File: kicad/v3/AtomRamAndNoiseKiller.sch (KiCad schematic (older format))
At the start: 26 parts, among them J1 Conn_01x10, J2 Conn_01x10, J3 Conn_01x03, J4 Conn_01x09, J5 Conn_01x09, J6 Conn_01x03, U1 74HCT14, U2 74HCT08, U3 74HCT245, U4 74HCT573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

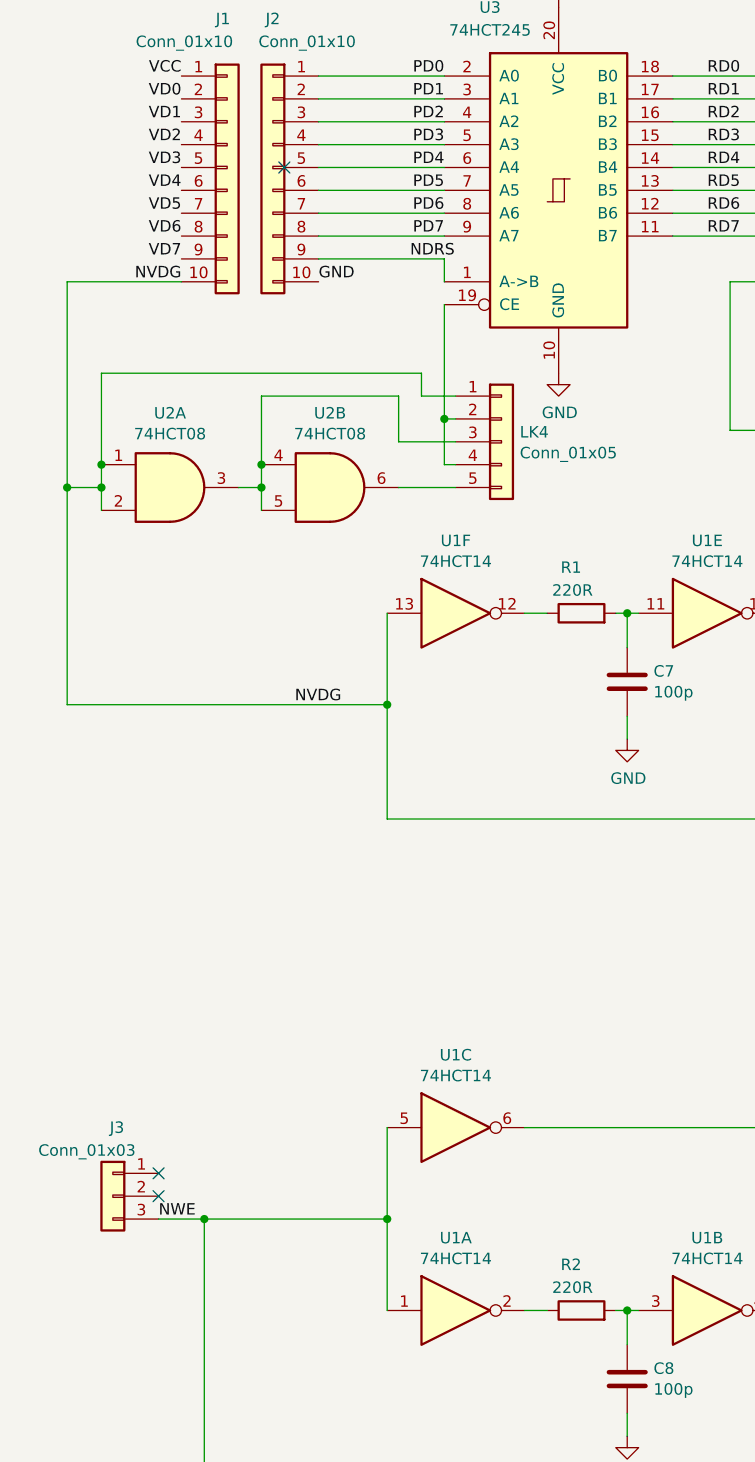
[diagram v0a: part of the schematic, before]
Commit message: Swapped NRDS and VDG on header
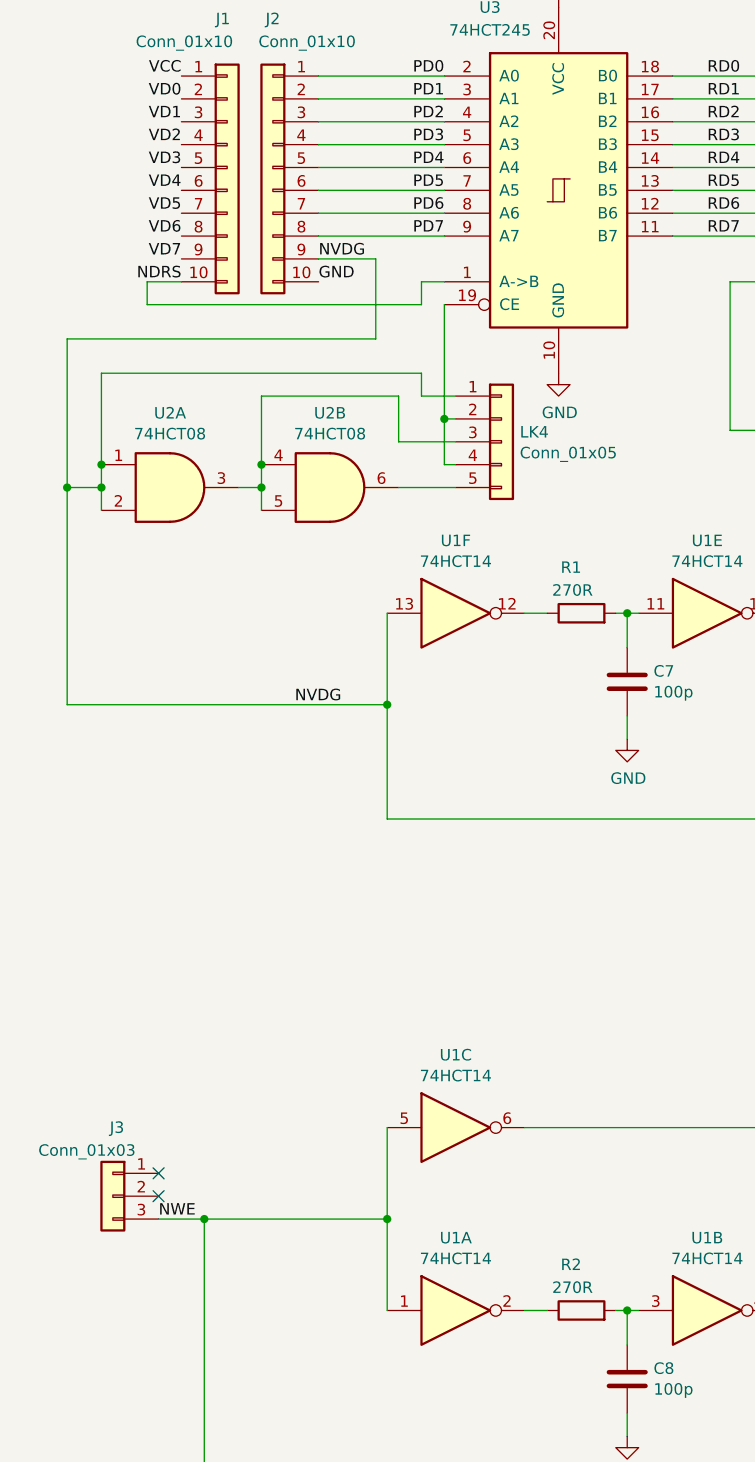
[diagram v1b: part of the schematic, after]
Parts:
- R1, R2: value 220R -> 270R
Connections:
- net NDRS: now also J1.10 (Pin_10); no longer J2.9 (Pin_9)
- net NVDG: now also J2.9 (Pin_9); no longer J1.10 (Pin_10)
- no-connect marks 9 -> 8
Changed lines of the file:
@@
 P 2950 3700
 F 0 "R1" V 3150 3700 50  0000 L CNN
-F 1 "220R" V 3050 3650 50  0000 L CNN
+F 1 "270R" V 3050 3650 50  0000 L CNN
 F 2 "Resistor_THT:R_Axial_DIN0207_L6.3mm_D2.5mm_P10.16mm_Horizontal" V 2880 3700 50  0001 C CNN
 F 3 "~" H 2950 3700 50  0001 C CNN
@@
 Text Label 2350 2050 2    50   ~ 0
 PD7
-Text Label 1200 2250 2    50   ~ 0
+Text Label 1800 2150 0    50   ~ 0
 NVDG
 $Comp
@@
 Text Label 6050 4300 0    50   ~ 0
 LOAD
-Text Label 2200 2150 0    50   ~ 0
+Text Label 1200 2250 2    50   ~ 0
 NDRS
 $Comp
@@
 $EndComp
 Connection ~ 10850 6250
-Wire Wire Line
-	2350 2250 2350 2150
-Wire Wire Line
-	2350 2150 1800 2150
-$Comp
-L Connector_Generic:Conn_01x10 J2
-U 1 1 5CB35F97
-P 1600 1750
-F 0 "J2" H 1600 2400 50  0000 C CNN
-F 1 "Conn_01x10" H 1450 2300 50  0000 C CNN
-F 2 "footprints:FinePinHeader_1x10_P2.54mm_Vertical" H 1600 1750 50  0001 C CNN
-F 3 "~" H 1600 1750 50  0001 C CNN
-	1    1600 1750
-	-1   0    0    -1
-$EndComp
 $Comp
 L Connector_Generic:Conn_01x10 J1
@@
 Wire Wire Line
 	700  4100 700  3150
-Wire Wire Line
-	700  2250 1200 2250
 $Comp
 L 74xx:74HC14 U1
@@
 	1    0    0    -1
 $EndComp
-NoConn ~ 1650 1750
 $Comp
 L Device:R R2
@@
 P 2950 6750
 F 0 "R2" V 3150 6750 50  0000 L CNN
-F 1 "220R" V 3050 6700 50  0000 L CNN
+F 1 "270R" V 3050 6700 50  0000 L CNN
 F 2 "Resistor_THT:R_Axial_DIN0207_L6.3mm_D2.5mm_P10.16mm_Horizontal" V 2880 6750 50  0001 C CNN
 F 3 "~" H 2950 6750 50  0001 C CNN
@@
 	2150 2750 2150 2950
 Wire Wire Line
-	700  2250 700  3150
-Wire Wire Line
 	850  3050 850  2650
 Wire Wire Line
@@
 	2350 3050 2400 3050
 Connection ~ 2350 2850
+Wire Wire Line
+	1200 2250 1050 2250
+Wire Wire Line
+	1050 2250 1050 2350
+Wire Wire Line
+	1050 2350 2250 2350
+Wire Wire Line
+	2250 2350 2250 2250
+Wire Wire Line
+	2250 2250 2350 2250
+Wire Wire Line
+	1800 2150 2050 2150
+Wire Wire Line
+	2050 2150 2050 2500
+Wire Wire Line
+	2050 2500 700  2500
+Wire Wire Line
+	700  2500 700  3150
+$Comp
+L Connector_Generic:Conn_01x10 J2
+U 1 1 5CB35F97
+P 1600 1750
+F 0 "J2" H 1600 2400 50  0000 C CNN
+F 1 "Conn_01x10" H 1450 2300 50  0000 C CNN
+F 2 "footprints:FinePinHeader_1x10_P2.54mm_Vertical" H 1600 1750 50  0001 C CNN
+F 3 "~" H 1600 1750 50  0001 C CNN
+	1    1600 1750
+	-1   0    0    -1
+$EndComp
 $EndSCHEMATC

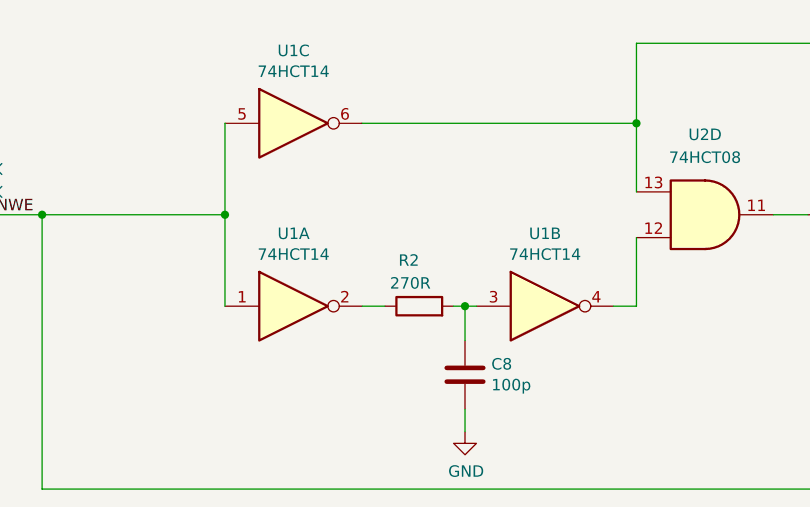
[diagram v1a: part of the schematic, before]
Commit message: Updated R2 from 270R to 1K0
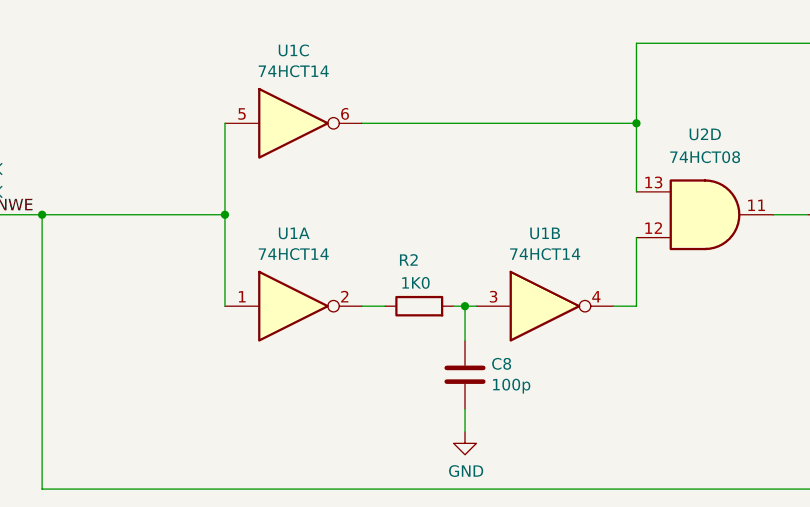
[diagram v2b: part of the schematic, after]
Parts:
- R2: value 270R -> 1K0
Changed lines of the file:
@@
 P 2950 6750
 F 0 "R2" V 3150 6750 50  0000 L CNN
-F 1 "270R" V 3050 6700 50  0000 L CNN
+F 1 "1K0" V 3050 6700 50  0000 L CNN
 F 2 "Resistor_THT:R_Axial_DIN0207_L6.3mm_D2.5mm_P10.16mm_Horizontal" V 2880 6750 50  0001 C CNN
 F 3 "~" H 2950 6750 50  0001 C CNN
